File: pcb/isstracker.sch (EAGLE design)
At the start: 22 parts, among them IC2 L7805CV, J1 MOTOR_RIGHT, J2 MOTOR, J3 MOTOR_LEFT, J4 DISPLAY, J6 CONTROL, J8 UART, J9 DISTANCE, Q2 60V/32A/35mΩ, U1 ARGON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

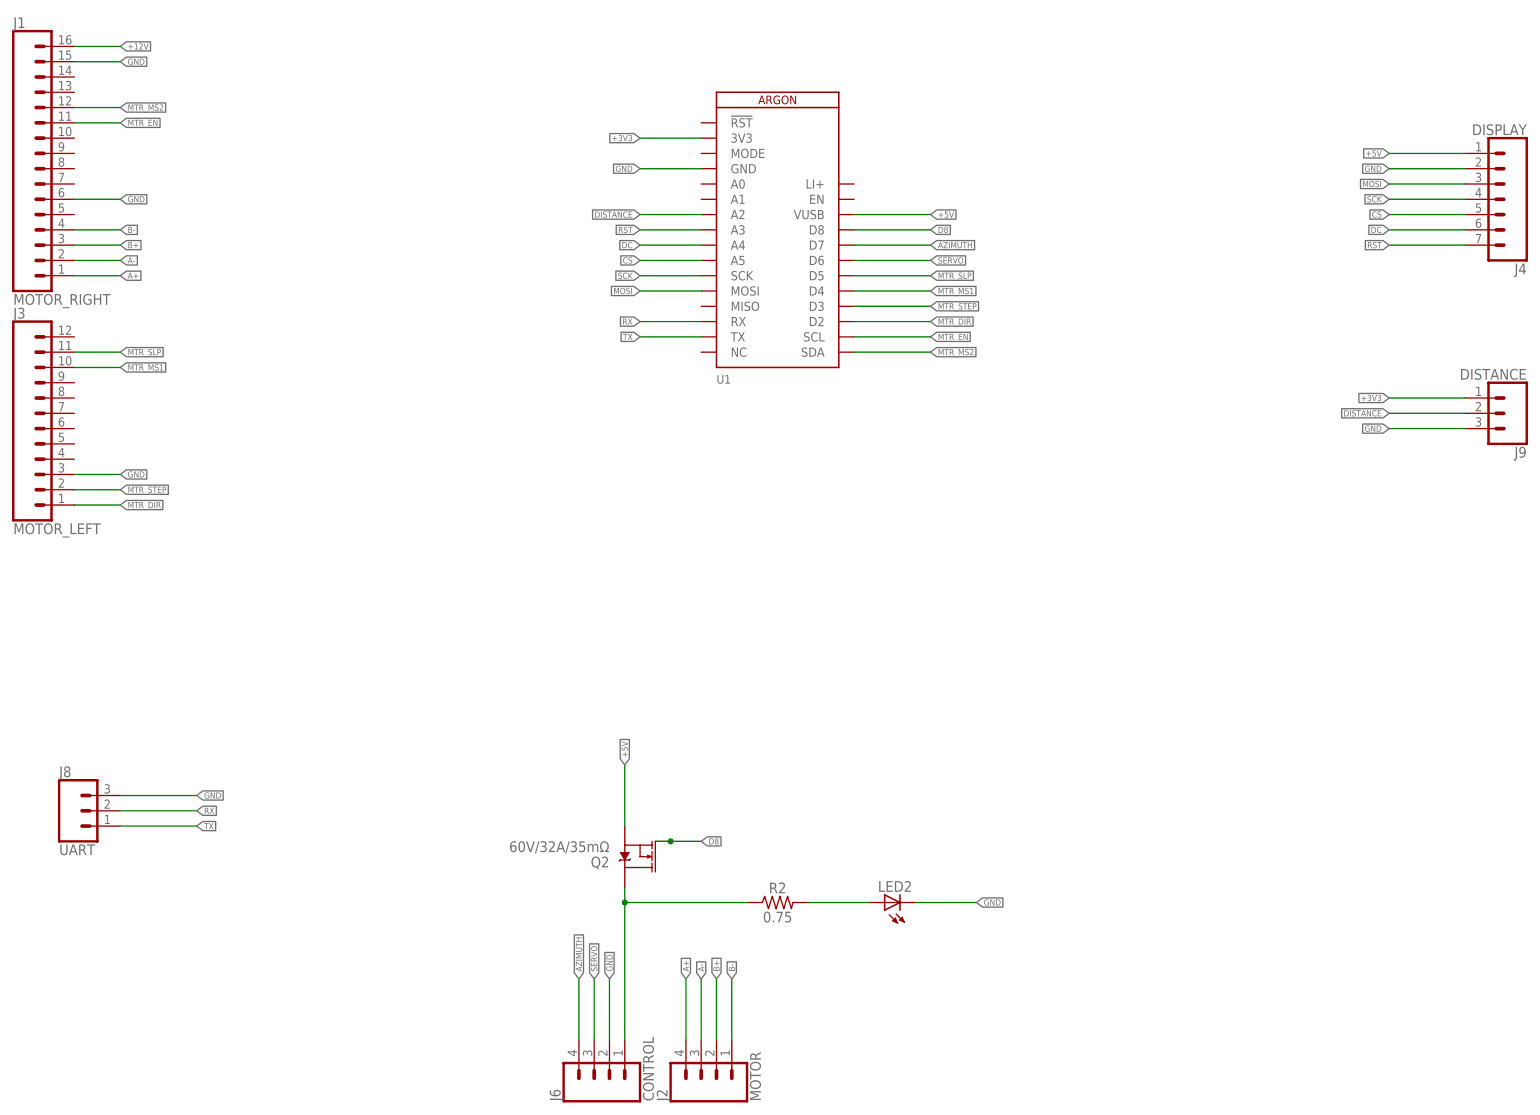
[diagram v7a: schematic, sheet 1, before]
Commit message: Layout tweaks
* Swap pth for smd LED's
* Move globe power pin to new location
* Add support hole for motor board if attached via headers
* Layout fixes for globe with new 4 pin setup
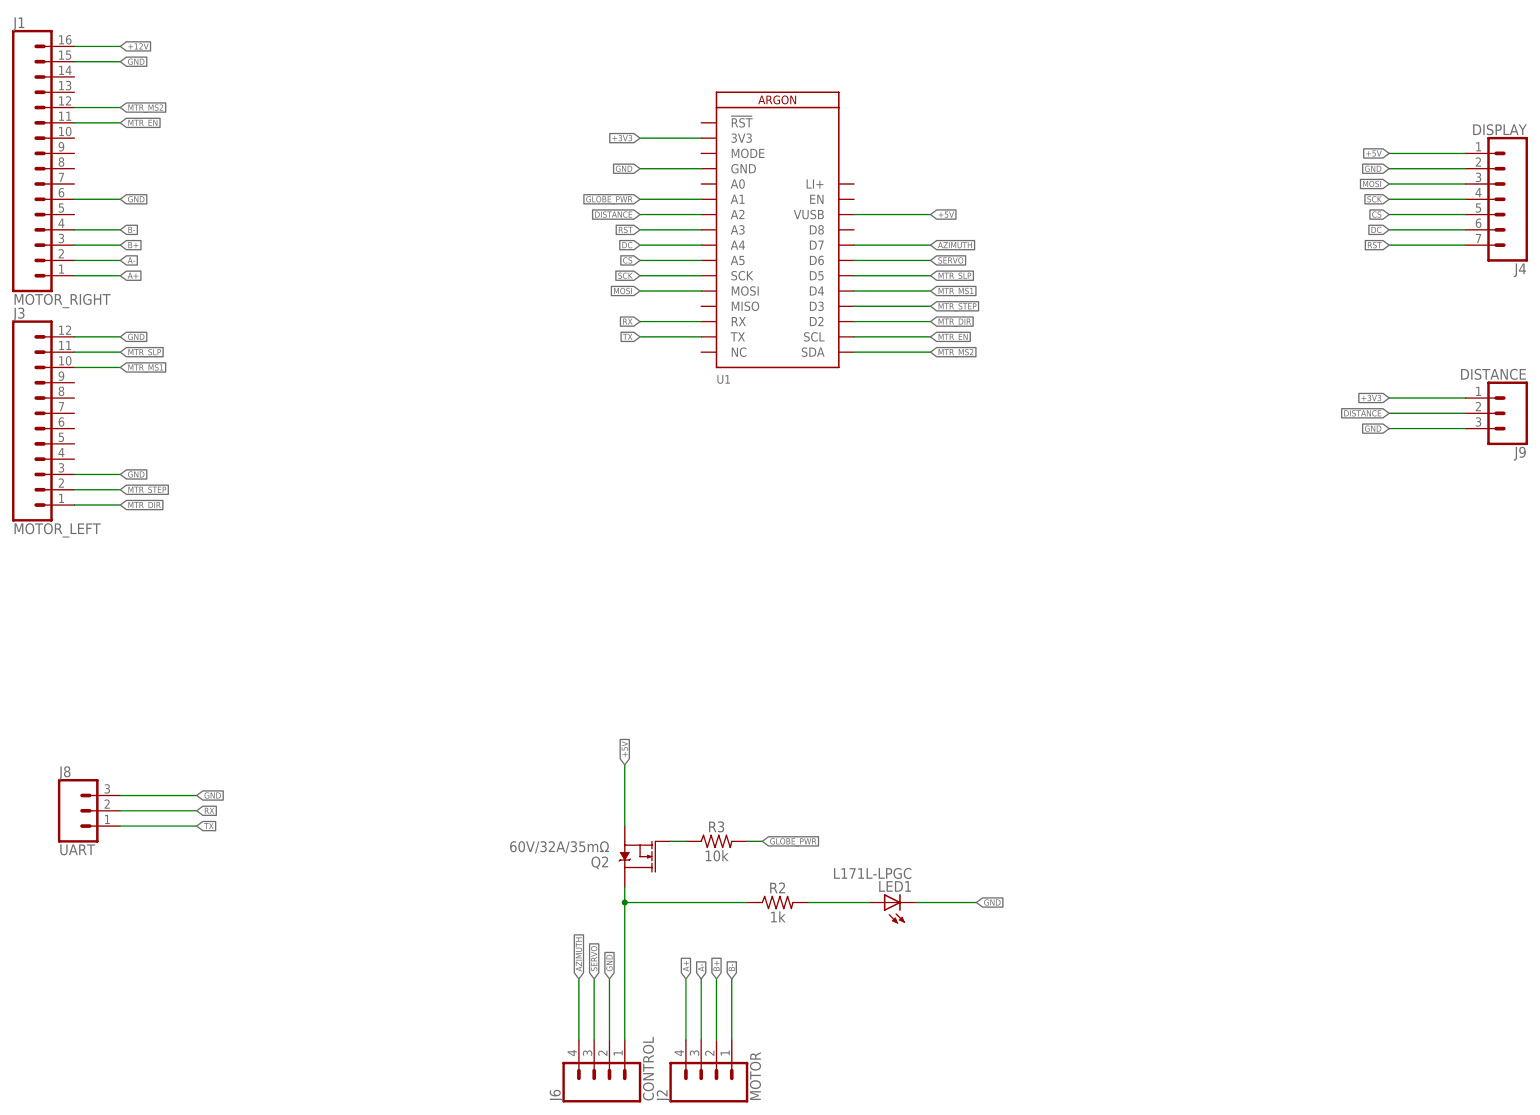
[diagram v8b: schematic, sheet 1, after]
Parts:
- removed LED2: (no value), adafruit:LED3MM
- added H6: MOUNT-HOLE2.8, holes:MOUNT-HOLE2.8
- added LED3: L171L-LPGC, adafruit:LEDCHIPLED_1206
- added R3: 10k, SparkFun-Resistors:0.75OHM-0805-1/4W-1%
- LED1: value RED -> L171L-LPGC; device adafruit:LED3MM -> adafruit:LEDCHIPLED_1206
- R2: value 0.75 -> 1k
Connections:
- removed net D8: Q2.G, U1.D8
- new net GLOBE_PWR: R3.2, U1.A1
- new net N$6: Q2.G, R3.1
- net GND: now also J3.12, LED3.C; no longer LED2.C
- net N$2: now also LED3.A; no longer LED1.A
- net N$4: now also LED1.A; no longer LED2.A
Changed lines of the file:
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@@
 <part name="D1" library="diode" library_urn="urn:adsk.eagle:library:210" deviceset="1N4004" device="" package3d_urn="urn:adsk.eagle:package:43336/1"/>
 <part name="IC2" library="linear" library_urn="urn:adsk.eagle:library:262" deviceset="78*" device="TV" package3d_urn="urn:adsk.eagle:package:16417/2" technology="05" value="L7805CV"/>
-<part name="LED1" library="adafruit" library_urn="urn:adsk.eagle:library:420" deviceset="LED" device="3MM" package3d_urn="urn:adsk.eagle:package:6240537/1" value="RED"/>
 <part name="R1" library="SparkFun-Resistors" library_urn="urn:adsk.eagle:library:532" deviceset="0.3OHM" device="-0805-1/8W-1%" package3d_urn="urn:adsk.eagle:package:39651/1" value="1k"/>
 <part name="C2" library="SparkFun-Capacitors" library_urn="urn:adsk.eagle:library:510" deviceset="100UF-POLAR" device="-RADIAL-2.5MM-25V-20%" package3d_urn="urn:adsk.eagle:package:37415/1" value="100uF"/>
@@
 <part name="J6" library="SparkFun-Connectors" library_urn="urn:adsk.eagle:library:513" deviceset="CONN_04" device="" package3d_urn="urn:adsk.eagle:package:38085/1" value="CONTROL"/>
 <part name="Q2" library="SparkFun-DiscreteSemi" library_urn="urn:adsk.eagle:library:514" deviceset="MOSFET-NCH" device="-FQP30N06L" package3d_urn="urn:adsk.eagle:package:38447/1" value="60V/32A/35mΩ"/>
-<part name="R2" library="SparkFun-Resistors" library_urn="urn:adsk.eagle:library:532" deviceset="0.75OHM" device="-0805-1/4W-1%" package3d_urn="urn:adsk.eagle:package:39651/1" value="0.75"/>
-<part name="LED2" library="adafruit" library_urn="urn:adsk.eagle:library:420" deviceset="LED" device="3MM" package3d_urn="urn:adsk.eagle:package:6240537/1"/>
+<part name="R2" library="SparkFun-Resistors" library_urn="urn:adsk.eagle:library:532" deviceset="0.75OHM" device="-0805-1/4W-1%" package3d_urn="urn:adsk.eagle:package:39651/1" value="1k"/>
+<part name="H6" library="holes" library_urn="urn:adsk.eagle:library:237" deviceset="MOUNT-HOLE" device="2.8" package3d_urn="urn:adsk.eagle:package:14271/1"/>
+<part name="R3" library="SparkFun-Resistors" library_urn="urn:adsk.eagle:library:532" deviceset="0.75OHM" device="-0805-1/4W-1%" package3d_urn="urn:adsk.eagle:package:39651/1" value="10k"/>
+<part name="LED3" library="adafruit" library_urn="urn:adsk.eagle:library:420" deviceset="LED" device="CHIPLED_1206" package3d_urn="urn:adsk.eagle:package:6240560/1" value="L171L-LPGC"/>
+<part name="LED1" library="adafruit" library_urn="urn:adsk.eagle:library:420" deviceset="LED" device="CHIPLED_1206" package3d_urn="urn:adsk.eagle:package:6240560/1" value="L171L-LPGC"/>
 </parts>
 <sheets>
@@
 <attribute name="VALUE" x="137.16" y="64.516" size="1.778" layer="96" font="vector" align="top-center"/>
 </instance>
-<instance part="LED2" gate="G$1" x="154.94" y="66.04" smashed="yes" rot="R90">
+<instance part="R3" gate="G$1" x="127" y="76.2" smashed="yes">
+<attribute name="NAME" x="127" y="77.724" size="1.778" layer="95" font="vector" align="bottom-center"/>
+<attribute name="VALUE" x="127" y="74.676" size="1.778" layer="96" font="vector" align="top-center"/>
+</instance>
+<instance part="LED1" gate="G$1" x="154.94" y="66.04" smashed="yes" rot="R90">
 <attribute name="NAME" x="159.512" y="69.596" size="1.778" layer="95" rot="R180"/>
 <attribute name="VALUE" x="159.512" y="71.755" size="1.778" layer="96" rot="R180"/>
@@
 </segment>
 <segment>
-<pinref part="LED2" gate="G$1" pin="C"/>
 <wire x1="160.02" y1="66.04" x2="170.18" y2="66.04" width="0.1524" layer="91"/>
 <label x="170.18" y="66.04" size="1.016" layer="95" xref="yes"/>
+<pinref part="LED1" gate="G$1" pin="C"/>
+</segment>
+<segment>
+<pinref part="J3" gate="G$1" pin="12"/>
+<wire x1="20.32" y1="160.02" x2="27.94" y2="160.02" width="0.1524" layer="91"/>
+<label x="27.94" y="160.02" size="1.016" layer="95" xref="yes"/>
 </segment>
 </net>
@@
 </segment>
 </net>
-<net name="D8" class="0">
-<segment>
-<wire x1="116.84" y1="76.2" x2="119.38" y2="76.2" width="0.1524" layer="91"/>
-<label x="124.46" y="76.2" size="1.016" layer="95" xref="yes"/>
+<net name="N$4" class="0">
+<segment>
+<pinref part="R2" gate="G$1" pin="2"/>
+<wire x1="142.24" y1="66.04" x2="152.4" y2="66.04" width="0.1524" layer="91"/>
+<pinref part="LED1" gate="G$1" pin="A"/>
+</segment>
+</net>
+<net name="N$6" class="0">
+<segment>
 <pinref part="Q2" gate="NMOS" pin="G"/>
-<wire x1="119.38" y1="76.2" x2="124.46" y2="76.2" width="0.1524" layer="91"/>
-<junction x="119.38" y="76.2"/>
-</segment>
-<segment>
-<pinref part="U1" gate="U1" pin="D8"/>
-<wire x1="149.86" y1="177.8" x2="162.56" y2="177.8" width="0.1524" layer="91"/>
-<label x="162.56" y="177.8" size="1.016" layer="95" xref="yes"/>
-</segment>
-</net>
-<net name="N$4" class="0">
-<segment>
-<pinref part="R2" gate="G$1" pin="2"/>
-<pinref part="LED2" gate="G$1" pin="A"/>
-<wire x1="142.24" y1="66.04" x2="152.4" y2="66.04" width="0.1524" layer="91"/>
+<pinref part="R3" gate="G$1" pin="1"/>
+<wire x1="119.38" y1="76.2" x2="121.92" y2="76.2" width="0.1524" layer="91"/>
+</segment>
+</net>
+<net name="GLOBE_PWR" class="0">
+<segment>
+<pinref part="U1" gate="U1" pin="A1"/>
+<wire x1="124.46" y1="182.88" x2="114.3" y2="182.88" width="0.1524" layer="91"/>
+<label x="114.3" y="182.88" size="1.016" layer="95" rot="R180" xref="yes"/>
+</segment>
+<segment>
+<pinref part="R3" gate="G$1" pin="2"/>
+<wire x1="134.62" y1="76.2" x2="132.08" y2="76.2" width="0.1524" layer="91"/>
+<label x="134.62" y="76.2" size="1.016" layer="95" xref="yes"/>
 </segment>
 </net>
@@
 <attribute name="VALUE" x="149.86" y="116.205" size="1.778" layer="96" rot="R180"/>
 </instance>
-<instance part="LED1" gate="G$1" x="157.48" y="96.52" smashed="yes">
-<attribute name="NAME" x="161.036" y="91.948" size="1.778" layer="95" rot="R90"/>
-<attribute name="VALUE" x="163.195" y="91.948" size="1.778" layer="96" rot="R90"/>
-</instance>
 <instance part="R1" gate="G$1" x="157.48" y="109.22" smashed="yes" rot="R90">
 <attribute name="NAME" x="155.956" y="109.22" size="1.778" layer="95" font="vector" rot="R90" align="bottom-center"/>
@@
 <attribute name="NAME" x="29.972" y="163.1442" size="1.778" layer="95"/>
 <attribute name="VALUE" x="29.972" y="160.0962" size="1.778" layer="96"/>
+</instance>
+<instance part="H6" gate="G$1" x="27.94" y="149.86" smashed="yes">
+<attribute name="NAME" x="29.972" y="150.4442" size="1.778" layer="95"/>
+<attribute name="VALUE" x="29.972" y="147.3962" size="1.778" layer="96"/>
+</instance>
+<instance part="LED3" gate="G$1" x="157.48" y="96.52" smashed="yes">
+<attribute name="NAME" x="161.036" y="91.948" size="1.778" layer="95" rot="R90"/>
+<attribute name="VALUE" x="163.195" y="91.948" size="1.778" layer="96" rot="R90"/>
 </instance>
 </instances>
@@
 </segment>
 <segment>
-<pinref part="LED1" gate="G$1" pin="C"/>
 <wire x1="157.48" y1="91.44" x2="157.48" y2="83.82" width="0.1524" layer="91"/>
 <label x="157.48" y="83.82" size="1.016" layer="95" rot="R270" xref="yes"/>
+<pinref part="LED3" gate="G$1" pin="C"/>
 </segment>
 </net>
@@
 <segment>
 <pinref part="R1" gate="G$1" pin="1"/>
-<pinref part="LED1" gate="G$1" pin="A"/>
 <wire x1="157.48" y1="104.14" x2="157.48" y2="99.06" width="0.1524" layer="91"/>
-</segment>
-</net>
+<pinref part="LED3" gate="G$1" pin="A"/>
+</segment>
+</net>
